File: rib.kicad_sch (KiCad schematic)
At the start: 102 parts, among them J1 RJ45_LED, J10 Conn_01x04_Male, J11 Screw_Terminal_01x02, J12 Screw_Terminal_01x02, J13 Screw_Terminal_01x02, J14 Conn_01x02_Male, J15 Conn_01x02_Male, J2 RJ45_LED, J3 RJ45_LED, J4 RJ45_LED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

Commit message: Oh yeah, resistor networks exist
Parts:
- removed R11, R12, R13, R14, R15, R16, R17, R18, R19, R20, R23, R24, R27, R28: 2k, Resistor_THT:R_Axial_DIN0207_L6.3mm_D2.5mm_P10.16mm_Horizontal, symbol Device:R
- removed R29, R30, R31, R32, R33, R34: 10k, Resistor_THT:R_Axial_DIN0207_L6.3mm_D2.5mm_P10.16mm_Horizontal, symbol Device:R
- added RN1: R_Network06, Resistor_THT:R_Array_SIP7, symbol Device:R_Network06
- added RN2, RN3, RN4: R_Network05, Resistor_THT:R_Array_SIP6, symbol Device:R_Network05
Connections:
- net 3.3V: now also RN1.1 (common)
- net GND: now also RN2.1 (common), RN3.1 (common), RN4.1 (common)
- net at OC6.5, U5.11 (Din): now also RN4.3 (R2)
- net at J2.4, OC3.5: now also RN3.2 (R1)
- net at J2.5, OC3.7: now also RN2.6 (R5)
- net at J3.5, J7.1 (Pin_1): now also RN1.2 (R1)
- net at J4.3, U1.24 (GPIO18): now also RN1.7 (R6)
- net at J4.4, U1.25 (GPIO19): now also RN1.6 (R5)
- net at J4.5, J7.2 (Pin_2): now also RN1.5 (R4)
- net at J2.3, OC5.5: now also RN3.6 (R5)
- net at J1.3, OC5.7: now also RN3.5 (R4)
- net at J1.4, OC1.5: now also RN2.3 (R2)
- net at J1.5, OC1.7: now also RN2.2 (R1)
- net at J1.6, OC2.7: now also RN2.4 (R3)
- net at J1.7, OC2.5: now also RN2.5 (R4)
- net at OC6.7, U5.13 (CLK): now also RN4.2 (R1)
- net at J3.3, U1.19 (GPIO14): now also RN1.4 (R3)
- net at J3.4, U1.20 (GPIO15): now also RN1.3 (R2)
- net at J2.6, OC4.7: now also RN3.3 (R2)
- net at J2.7, OC4.5: now also RN3.4 (R3)
- net at OC7.5, U1.16 (GPIO12): now also RN4.5 (R4)
- net at OC7.7, U5.10 (~{CS}/SHDN): now also RN4.4 (R3)

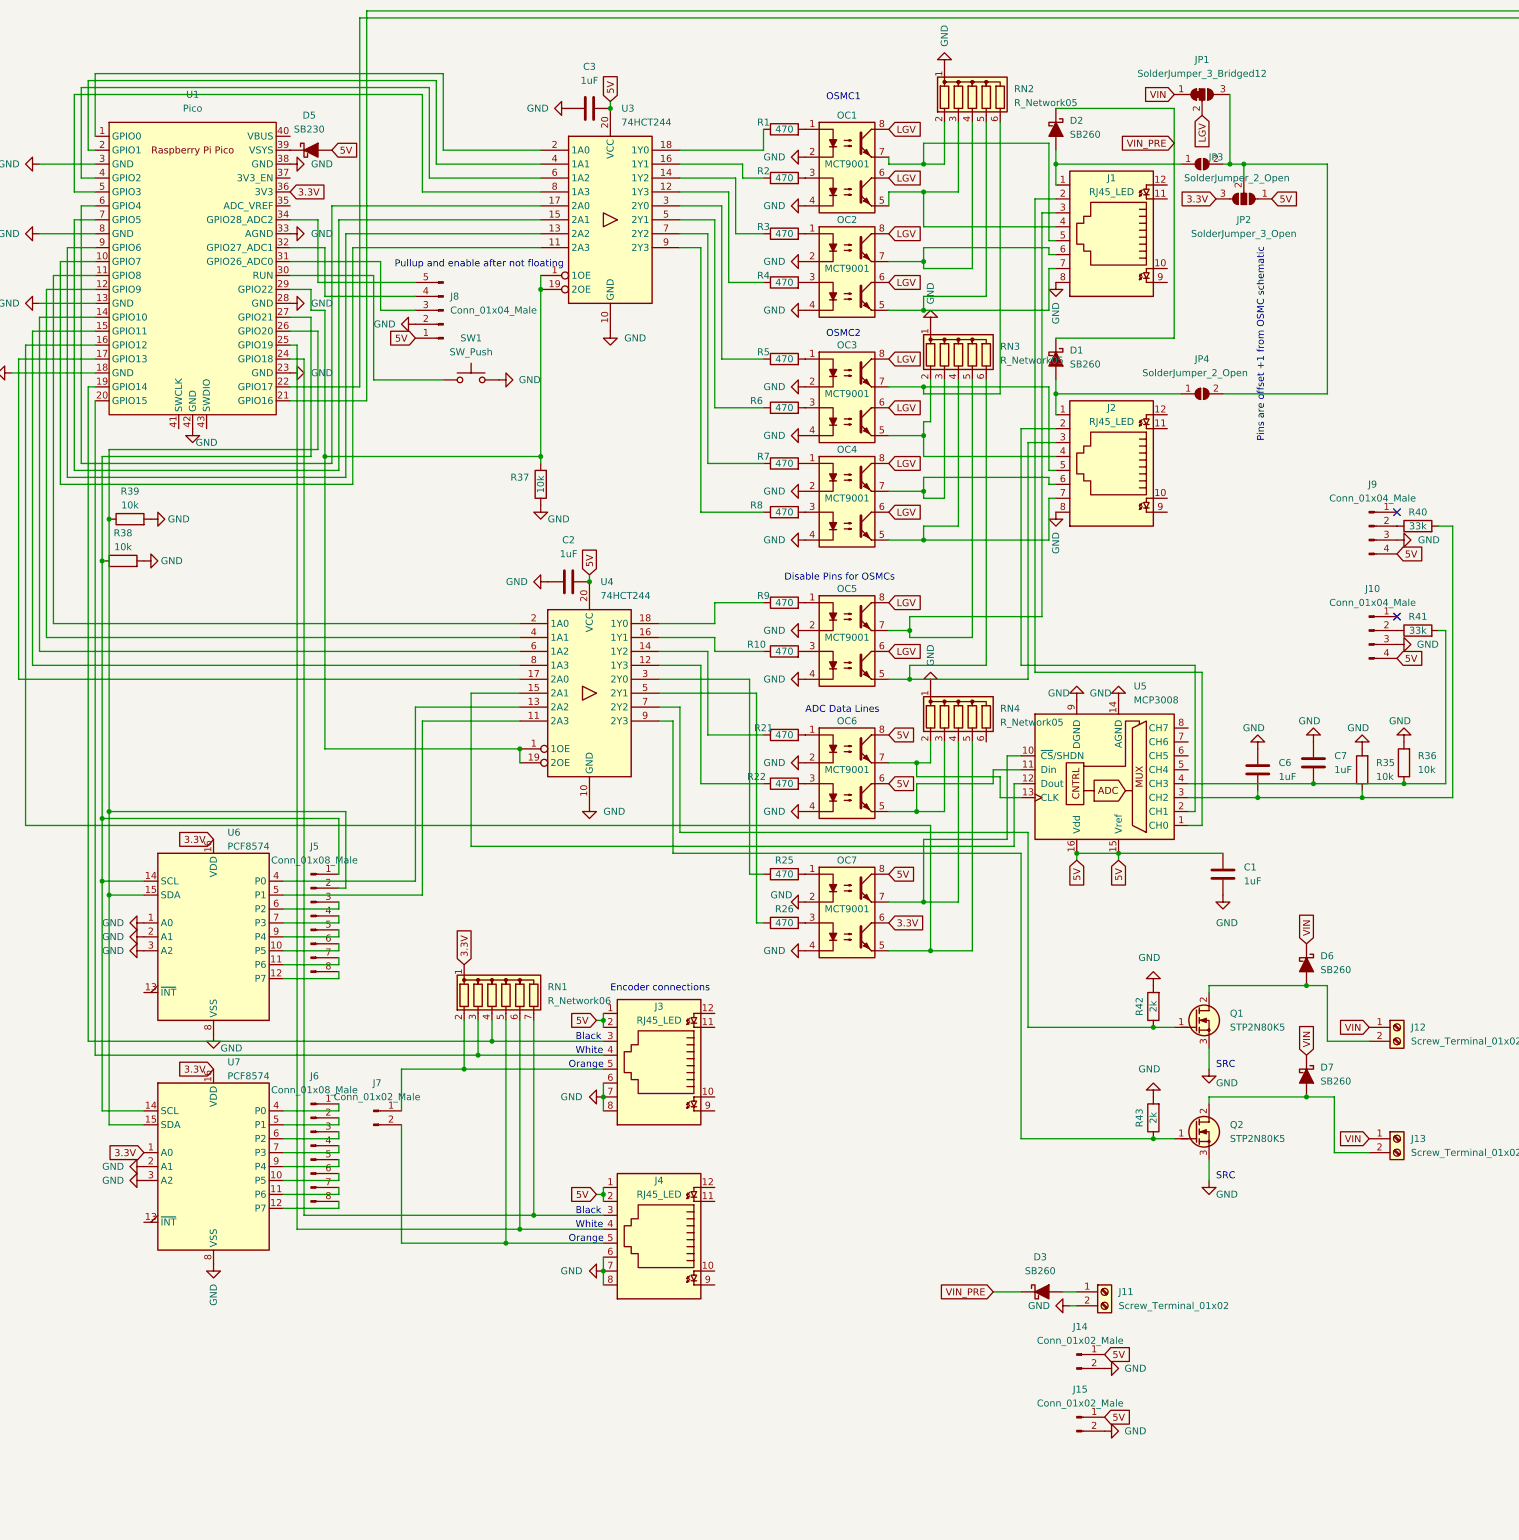
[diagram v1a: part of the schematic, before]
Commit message: Start adding led driver
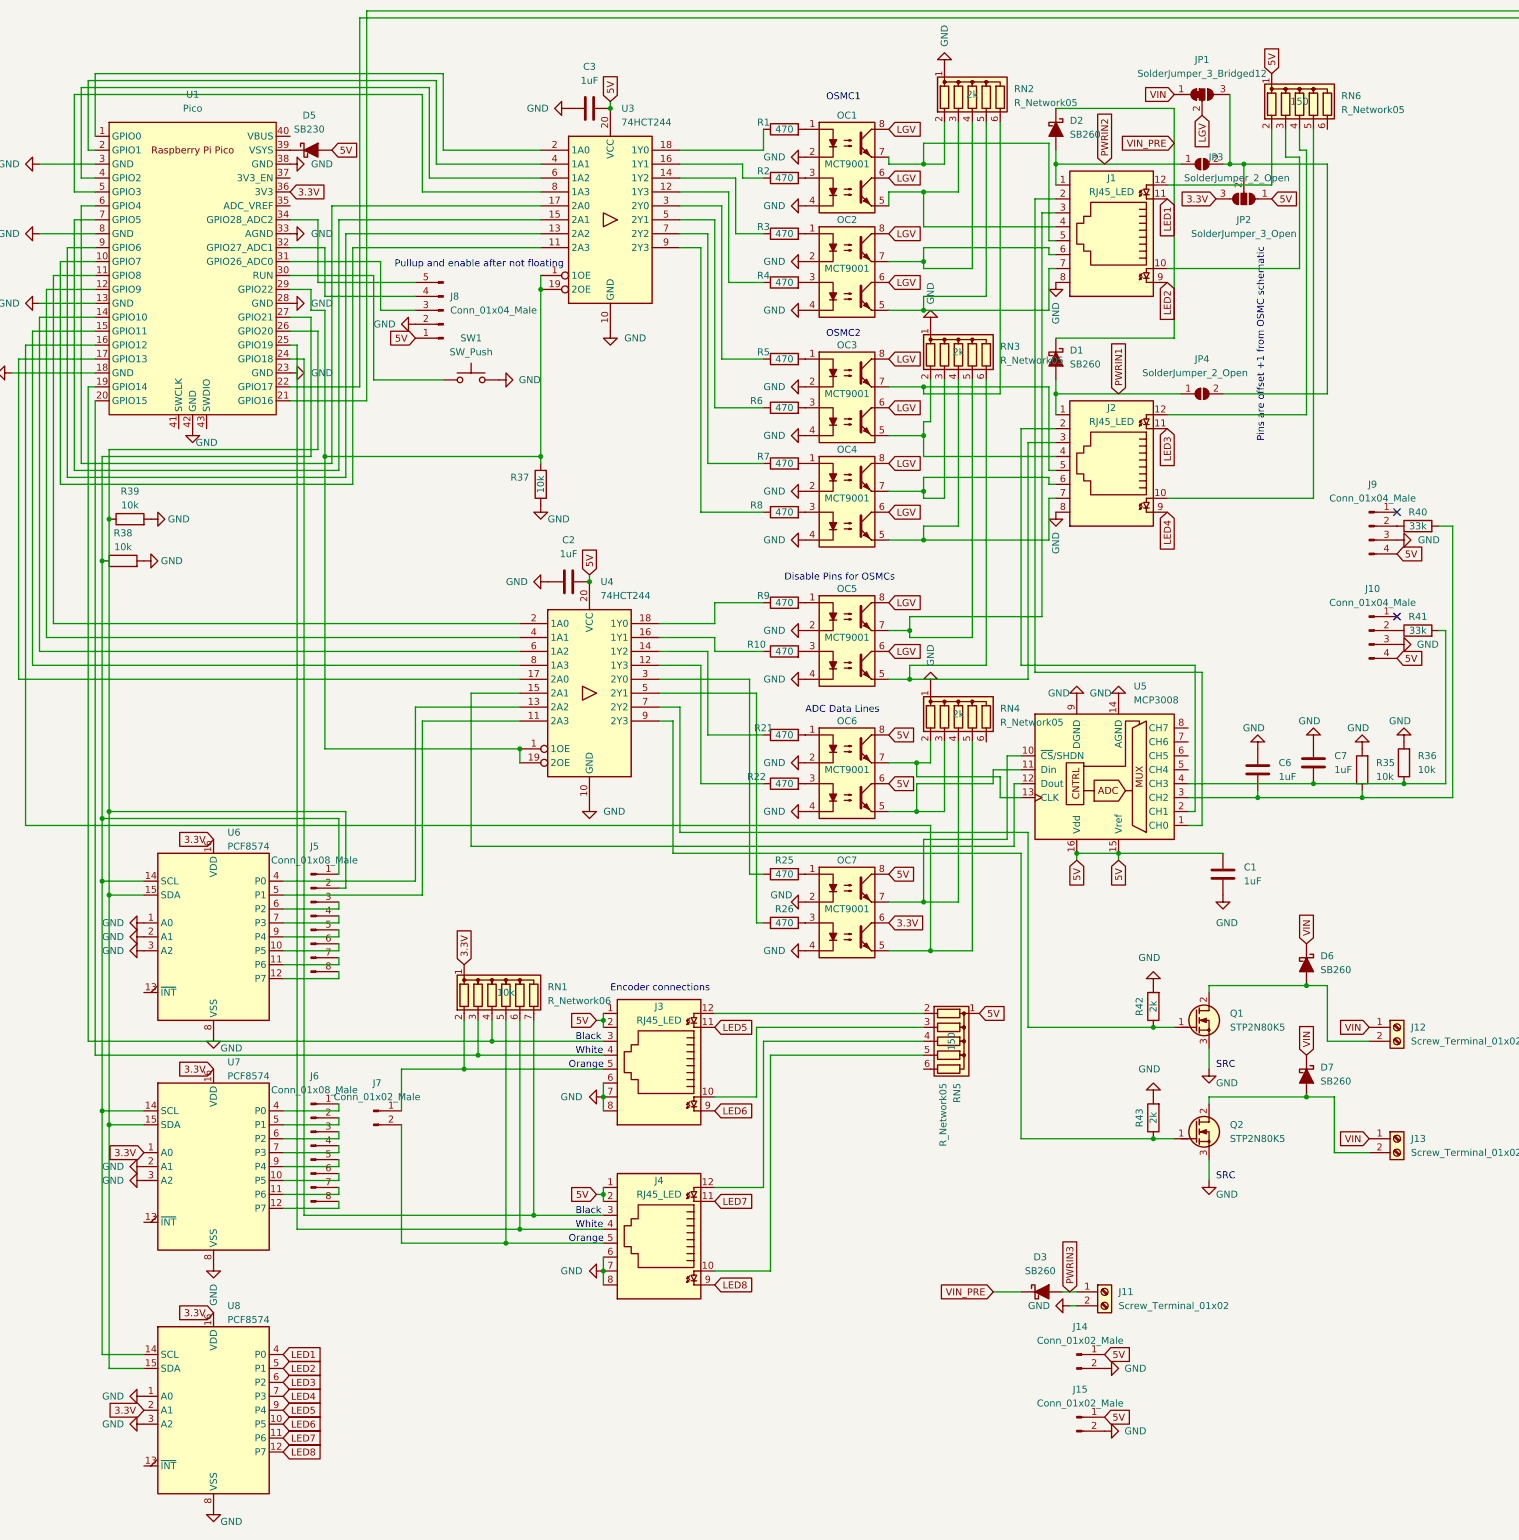
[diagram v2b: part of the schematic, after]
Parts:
- added RN5, RN6: R_Network05, Resistor_THT:R_Array_SIP6, symbol Device:R_Network05
- added U8: PCF8574, Package_DIP:DIP-16_W7.62mm_Socket, symbol Interface_Expansion:PCF8574
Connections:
- net 3.3V: now also U8.16 (VDD), U8.2 (A1)
- net 5V: now also RN5.1 (common), RN6.1 (common)
- net GND: now also U8.1 (A0), U8.3 (A2), U8.8 (VSS)
- net PWRIN2: now reaches D2.2 (A), J1.1, JP3.1 (A)
- net at J4.10: now also RN5.5 (R4)
- net LED7: now reaches J4.11
- net LED7: now also U8.11 (P6)
- net at J4.12: now also RN5.4 (R3)
- net LED8: now reaches J4.9
- net LED8: now also U8.12 (P7)
- net PWRIN1: now reaches D1.2 (A), J2.1, JP4.1 (A)
- net at J1.10: now also RN6.3 (R2)
- net LED1: now reaches J1.11
- net LED1: now also U8.4 (P0)
- net at J1.12: now also RN6.2 (R1)
- net LED2: now reaches J1.9
- net LED2: now also U8.5 (P1)
- net PWRIN3: now reaches D3.2 (A), J11.1 (Pin_1)
- net at J3.10: now also RN5.3 (R2)
- net LED5: now reaches J3.11
- net LED5: now also U8.9 (P4)
- net at J3.12: now also RN5.2 (R1)
- net LED6: now reaches J3.9
- net LED6: now also U8.10 (P5)
- net at J5.1 (Pin_1), R38.1, U1.27 (GPIO21)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: now also U8.14 (SCL)
- net at J5.2 (Pin_2), R39.1, U1.26 (GPIO20)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: now also U8.15 (SDA)
- net at J2.10: now also RN6.5 (R4)
- net LED3: now reaches J2.11
- net LED3: now also U8.6 (P2)
- net at J2.12: now also RN6.4 (R3)
- net LED4: now reaches J2.9
- net LED4: now also U8.7 (P3)

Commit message: Add 7seg, LED driver, connect LEDs. Fix BOM & add LEDs tomorrow
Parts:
- removed RN5, RN6: R_Network05, Resistor_THT:R_Array_SIP6, symbol Device:R_Network05
- removed U8: PCF8574, Package_DIP:DIP-16_W7.62mm_Socket, symbol Interface_Expansion:PCF8574
- added J16: Conn_01x06_Male, Connector_PinHeader_2.54mm:PinHeader_1x06_P2.54mm_Vertical, symbol Connector:Conn_01x06_Male
- added U8: MAX6959AAEE+, Package_DIP:DIP-16_W7.62mm_Socket, symbol MAX6959:MAX6959AAEE+
- added U9: DC56-11EWA, Display_7Segment:DA56-11SURKWA, symbol Display_Character:DC56-11EWA
- J8: value Conn_01x04_Male -> Conn_01x05_Male
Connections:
- net 5V: now also J16.1 (Pin_1), U8.16 (V+)
- net GND: now also J16.2 (Pin_2), U8.8 (GND)
- net LED1: now also U8.7 (DIG3/SEG3), U9.12 (DIG2_F), U9.18 (DIG1_F)
- net LED2: now also U8.15 (SEG8), U9.11 (DIG2_A), U9.16 (DIG1_A)
- net LED3: now also U8.14 (SEG7), U9.10 (DIG2_B), U9.15 (DIG1_B)
- net LED4: now also U8.13 (SEG6), U9.3 (DIG1_C), U9.8 (DIG2_C)
- net LED5: now also U8.12 (SEG5), U9.2 (DIG1_D), U9.6 (DIG2_D)
- net LED6: now also U8.11 (SEG4), U9.1 (DIG1_E), U9.5 (DIG2_E)
- net LED7: now also U8.5 (DIG1/SEG1), U9.13 (DIG2_CC), U9.4 (DP1)
- net LED8: now also U8.4 (DIG0/SEG0), U9.14 (DIG1_CC), U9.9 (DP2)
- net CATHODE3: now reaches J4.10
- net CATHODE3: now also J1.10, J1.12, J2.10, J2.12, J3.10, J3.12, J4.12, U8.6 (DIG2/SEG2), U9.17 (DIG1_G), U9.7 (DIG2_G)
- net SCL: now reaches J5.1 (Pin_1), R38.1, U1.27 (GPIO21), U6.14 (SCL), U7.14 (SCL)
- net SCL: now also U8.2 (SCL)
- net SDA: now reaches J5.2 (Pin_2), R39.1, U1.26 (GPIO20), U6.15 (SDA), U7.15 (SDA)
- net SDA: now also U8.1 (SDA)
- net at U5.5 (CH4): now also J16.3 (Pin_3)
- net at U5.6 (CH5): now also J16.4 (Pin_4)
- net at U5.7 (CH6): now also J16.5 (Pin_5)
- net at U5.8 (CH7): now also J16.6 (Pin_6)
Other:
- moved on the sheet: C4, C5, D4, H1, H2, H3, H4, H5, H6, L1, SW2, U2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

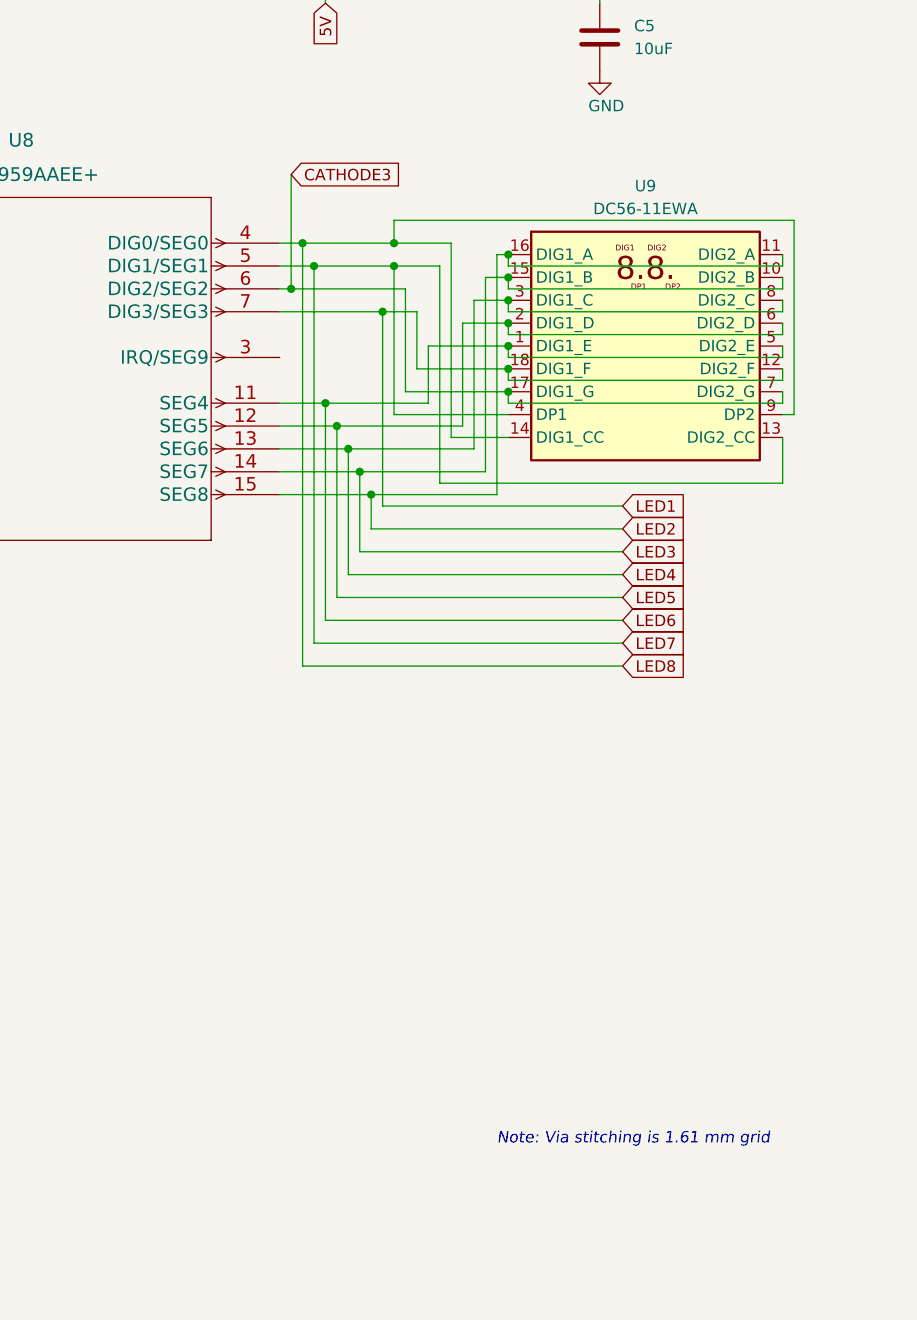
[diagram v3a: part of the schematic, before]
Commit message: Add RGB LEDs
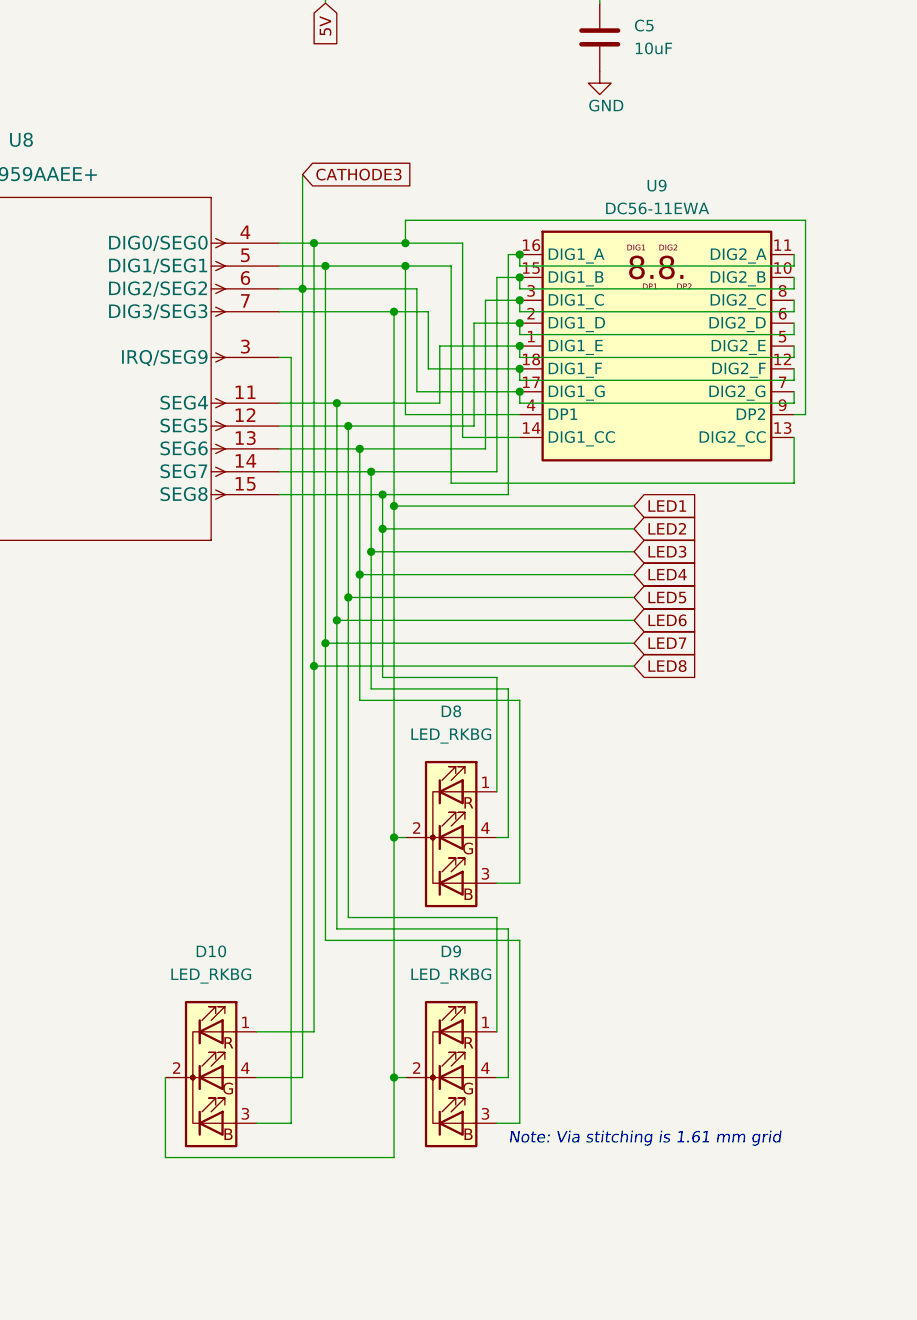
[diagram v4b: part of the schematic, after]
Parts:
- added D10, D8, D9: LED_RKBG, LED_THT:LED_D5.0mm-4_RGB, symbol Device:LED_RKBG
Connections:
- net CATHODE3: now also D10.4 (GA)
- net LED1: now also D10.2 (K), D8.2 (K), D9.2 (K)
- net LED2: now also D8.1 (RA)
- net LED3: now also D8.4 (GA)
- net LED4: now also D8.3 (BA)
- net LED5: now also D9.1 (RA)
- net LED6: now also D9.4 (GA)
- net LED7: now also D9.3 (BA)
- net LED8: now also D10.1 (RA)
- net at U8.3 (IRQ/SEG9): now also D10.3 (BA)
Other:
- moved on the sheet: U9

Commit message: Add RGB LEDs
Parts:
- D10, D8, D9: footprint LED_THT:LED_D5.0mm-4_RGB -> LED_THT:LED_D5.0mm-4_RGB_Staggered_Pins
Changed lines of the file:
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@@
     (property "Reference" "D9" (id 0) (at 365.76 224.79 0))
     (property "Value" "LED_RKBG" (id 1) (at 365.76 227.33 0))
-    (property "Footprint" "LED_THT:LED_D5.0mm-4_RGB" (id 2) (at 365.76 240.03 0)
+    (property "Footprint" "LED_THT:LED_D5.0mm-4_RGB_Staggered_Pins" (id 2) (at 365.76 240.03 0)
       (effects (font (size 1.27 1.27)) hide)
     )
@@
     (property "Reference" "D8" (id 0) (at 365.76 198.12 0))
     (property "Value" "LED_RKBG" (id 1) (at 365.76 200.66 0))
-    (property "Footprint" "LED_THT:LED_D5.0mm-4_RGB" (id 2) (at 365.76 213.36 0)
+    (property "Footprint" "LED_THT:LED_D5.0mm-4_RGB_Staggered_Pins" (id 2) (at 365.76 213.36 0)
       (effects (font (size 1.27 1.27)) hide)
     )
@@
     (property "Reference" "D10" (id 0) (at 339.09 224.79 0))
     (property "Value" "LED_RKBG" (id 1) (at 339.09 227.33 0))
-    (property "Footprint" "LED_THT:LED_D5.0mm-4_RGB" (id 2) (at 339.09 240.03 0)
+    (property "Footprint" "LED_THT:LED_D5.0mm-4_RGB_Staggered_Pins" (id 2) (at 339.09 240.03 0)
       (effects (font (size 1.27 1.27)) hide)
     )
@@
     )
     (path "/841fcbc3-9bb3-4695-a72b-2bcdbe5e5fed"
-      (reference "D8") (unit 1) (value "LED_RKBG") (footprint "LED_THT:LED_D5.0mm-4_RGB")
+      (reference "D8") (unit 1) (value "LED_RKBG") (footprint "LED_THT:LED_D5.0mm-4_RGB_Staggered_Pins")
     )
     (path "/63087395-688c-4043-806a-33356104a228"
-      (reference "D9") (unit 1) (value "LED_RKBG") (footprint "LED_THT:LED_D5.0mm-4_RGB")
+      (reference "D9") (unit 1) (value "LED_RKBG") (footprint "LED_THT:LED_D5.0mm-4_RGB_Staggered_Pins")
     )
     (path "/b8b5796e-31a3-463f-9b4a-ebd188f27515"
-      (reference "D10") (unit 1) (value "LED_RKBG") (footprint "LED_THT:LED_D5.0mm-4_RGB")
+      (reference "D10") (unit 1) (value "LED_RKBG") (footprint "LED_THT:LED_D5.0mm-4_RGB_Staggered_Pins")
     )
     (path "/46ae22cd-43b5-4b2f-bb6e-c4094d5bd302"
